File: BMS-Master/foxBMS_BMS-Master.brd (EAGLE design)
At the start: 160 x 120 mm, 318 parts, among them IC1001 AQV252G2S, IC1002 AQV252G2S, IC1003 AQV252G2S, IC1004 AQV252G2S, IC1005 AQV252G2S, IC1006 AQV252G2S, IC1101 UA78L05ACPK, IC1102 ADUM1300ARW, IC1103 ADUM1300ARW, IC1401 IP4220CZ6, IC1402 FT231XS-R, IC1403 ADUM1401ARW, IC1404 IP4220CZ6, IC1405 FT231XS-R, IC1406 ADUM1401ARW, IC1501 AT25128B-SSHL-T, IC1801 IS42S16400J-5TL, IC201 LM1085IS-5.0/NOPB, IC202 MURATA_NCS6S1205C, IC301 LM1085IS-5.0/NOPB, IC302 RS-2405D/H2, IC401 ADR3425ARJZ, IC402 STM32F429IIT6, IC501 STM32F429VIT6, IC601 ADUM1401ARW, IC701 UA78L05ACPK, IC702 ADUM1301ARW, IC801 KA7805ERTF, IC802 TJA1052IT/1Y, IC803 CPC1008N, IC901 LM317MBSTT3G, IC902 CPC1008N, IC903 CPC1008N, IC904 CPC1008N, IC905 CPC1008N, Q401 7B-8.000MAAJ-T, Q501 7B-8.000MAAJ-T, T1001 IRLML0100TRPBF, T1002 IRLML0100TRPBF, T1003 IRLML0100TRPBF, T1004 IRLML0100TRPBF, T1005 IRLML0100TRPBF, T1006 IRLML0100TRPBF, T201 TISP40XXH1BJ, T401 BSS84P, T501 BSS84P, T701 IRLML0100TRPBF, T801 IRLML0100TRPBF, T901 BUK964R8-60E, T902 IRLML0100TRPBF, T903 IRLML0100TRPBF, X1201 43045-0400_MOLEX_4PIN, X1202 43045-0400_MOLEX_4PIN, X1203 43045-0400_MOLEX_4PIN, X1204 43045-0400_MOLEX_4PIN, X1205 43045-0400_MOLEX_4PIN, X1206 43045-0400_MOLEX_4PIN, X1401 MINI-USB-2.0, X1402 MINI-USB-2.0, X1601 43045-1600_MOLEX_16PIN, X201 43045-0600_MOLEX_6PIN, X402 MA02-1, X403 SAMTEC_FTS_20POL_HEADER_VERTI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, X501 MA02-1, X502 SAMTEC_FTS_20POL_HEADER_VERTI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, X701 43045-0400_MOLEX_4PIN, X801 43045-0400_MOLEX_4PIN, X901 43045-0200_MOLEX_2PIN, X902 MA02-1SMALL_PINS_OUTLINE

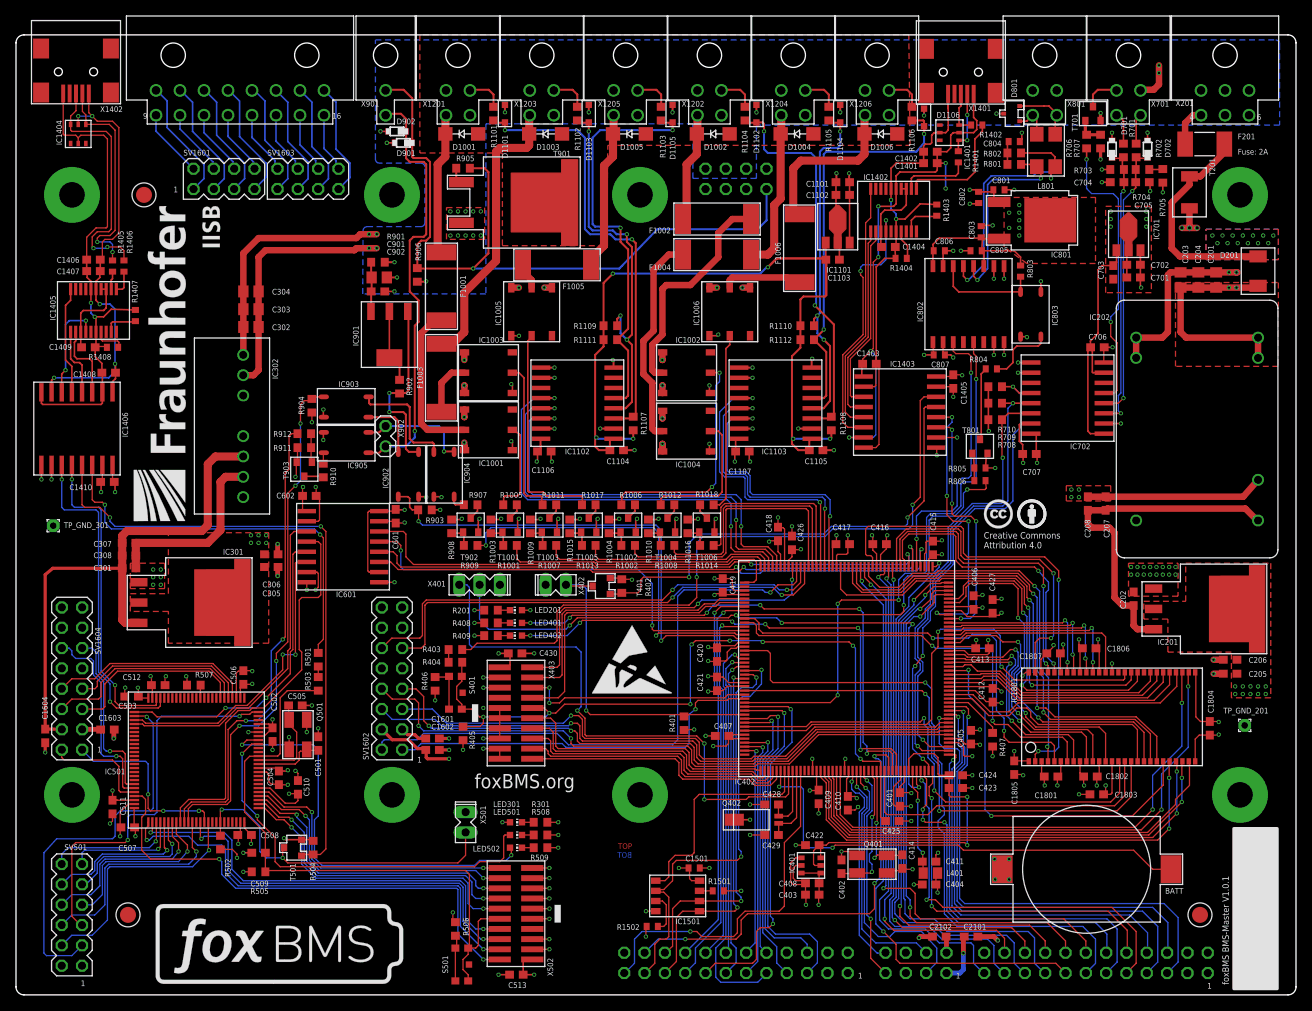
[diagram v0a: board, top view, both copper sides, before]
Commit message: updated foxBMS-slave to version 2.02
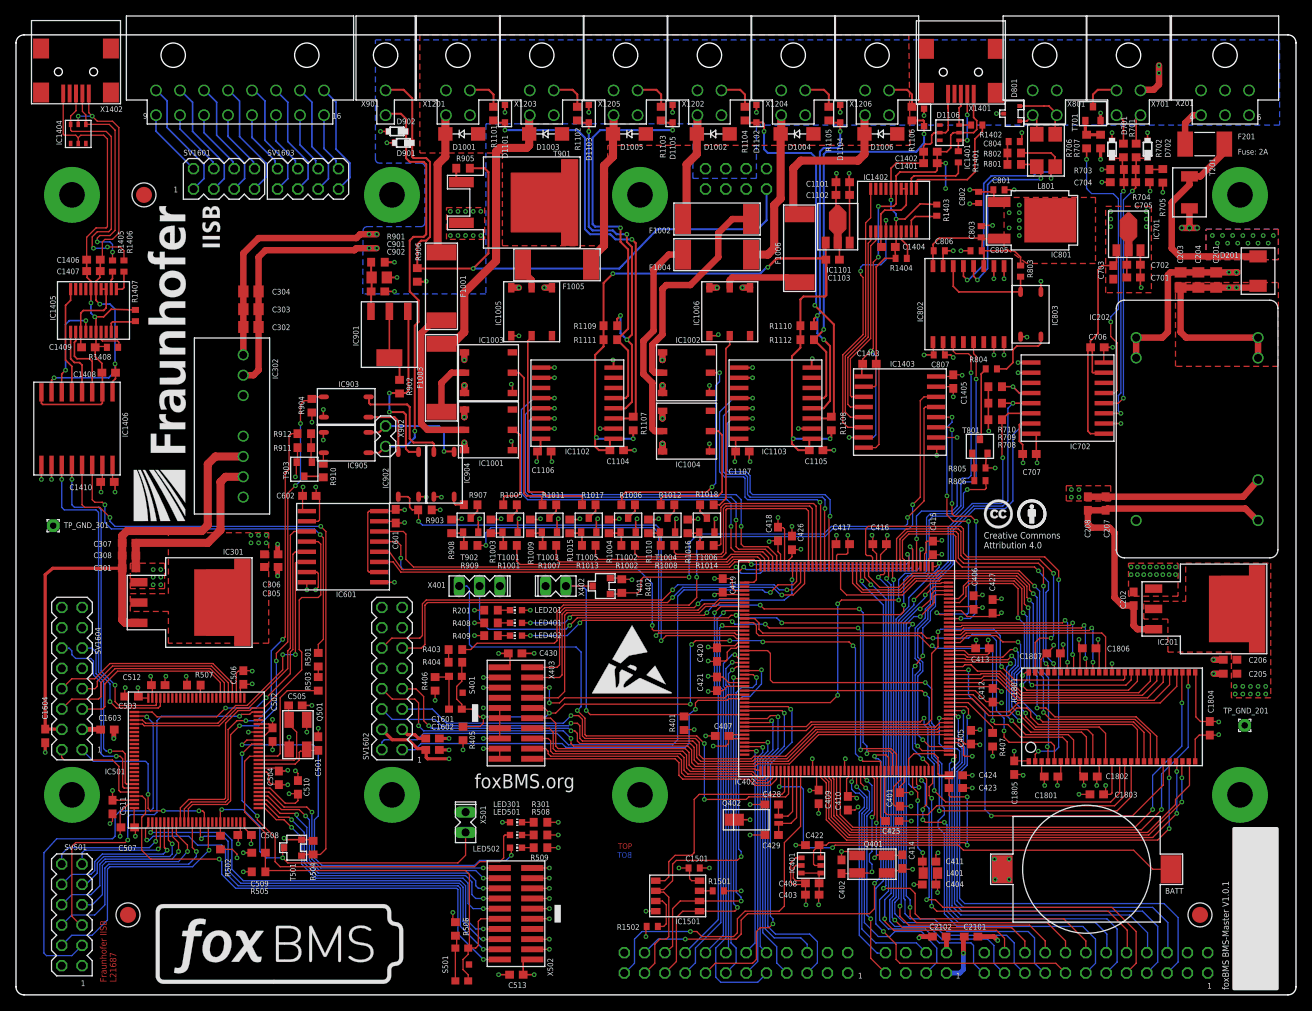
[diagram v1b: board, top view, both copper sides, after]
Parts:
- moved X401 0.16 mm to (57.9, -68.9)
- moved X402 0.16 mm to (67.5, -68.9)
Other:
- board text added: "Fraunhofer IISB L21584"
- board text added: "Fraunhofer IISB L21687"
